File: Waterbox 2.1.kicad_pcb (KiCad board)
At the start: 2 copper layers, 130.2 x 78.5 mm, 25 parts

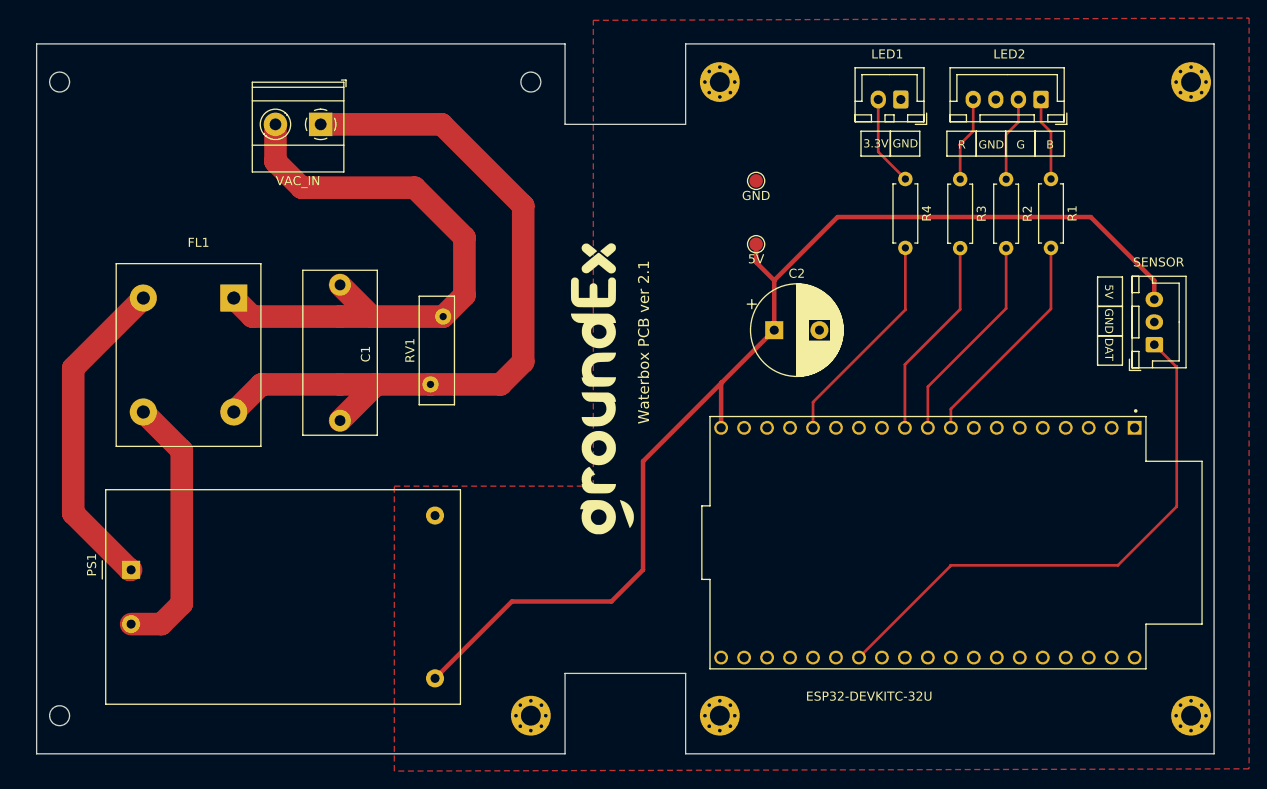
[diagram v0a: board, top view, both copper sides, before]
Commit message: route tracks in back copper, adding dc jack for additional dc power connector
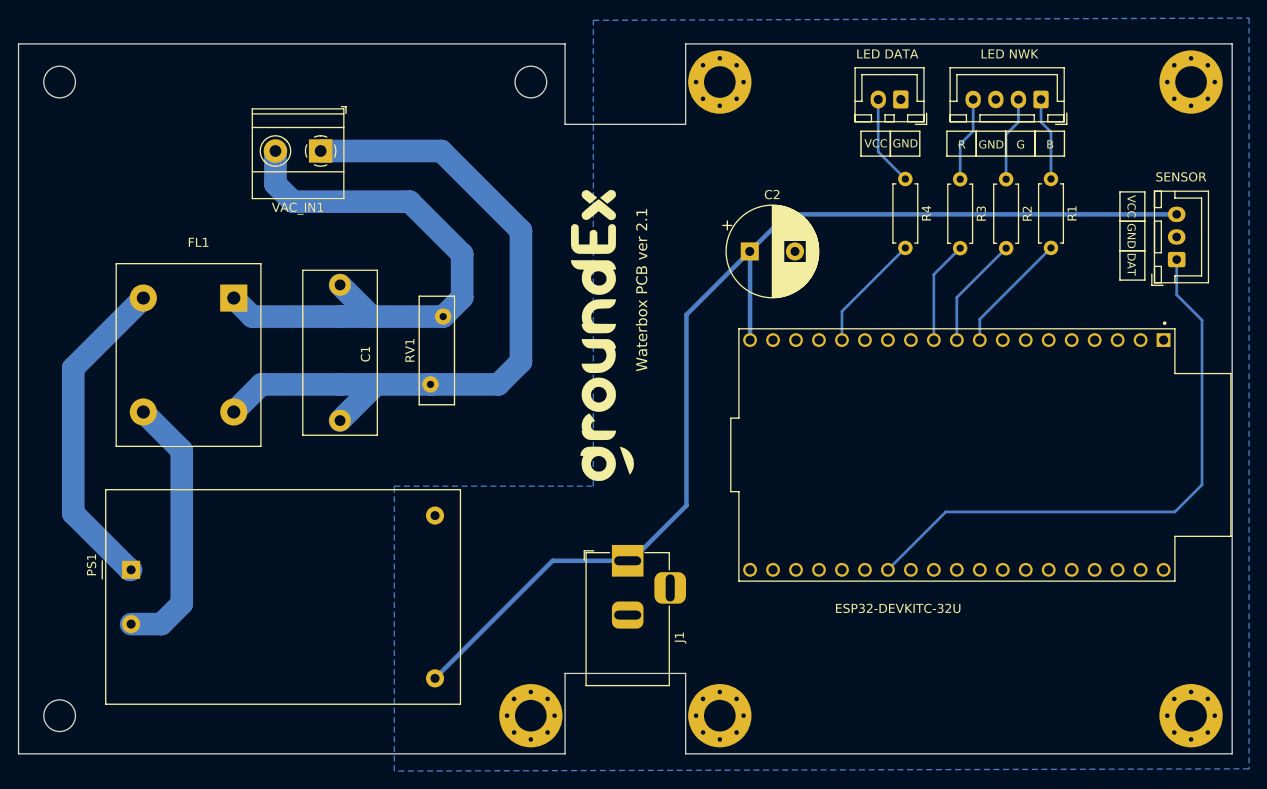
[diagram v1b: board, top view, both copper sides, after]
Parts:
- removed 5V: TP1, TestPoint:TestPoint_Pad_D1.5mm
- removed GND: TP2, TestPoint:TestPoint_Pad_D1.5mm
- added J1: Jack-DC, Connector_BarrelJack:BarrelJack_Horizontal, F.Cu at (125.8, 110.0)
- H1, H2, H3: footprint MountingHole:MountingHole_2.2mm_M2_ISO14580 -> MountingHole:MountingHole_3.5mm
- H4, H5, H6, H7, H8: footprint MountingHole:MountingHole_2.2mm_M2_Pad_Via -> MountingHole:MountingHole_3.5mm_Pad_Via
- LED DATA: renamed from LED1
- LED NWK: renamed from LED2
- moved ESP32-DEVKITC-32U 10.2 mm to (162.2, 98.3)
- moved SENSOR 9.73 mm to (186.5, 76.7)
- moved C2 9.11 mm to (139.3, 75.8)
- moved G*** 5.90 mm to (123.0, 85.1)
- moved VAC_IN1 2.94 mm to (91.9, 64.7)
- renumbered VAC_IN to VAC_IN1
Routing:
- net /LED_TEL: track 24.1 -> 13.1 mm
- net /RGBLED_R: track 22.4 -> 11.4 mm
- net /RGBLED_B: track 24.5 -> 13.4 mm
- net /RGBLED_G: track 23.4 -> 12.4 mm
- net /Sensor_Data: track 61.1 -> 64.7 mm
- net Net-(VAC_IN1-Pin_1): track 83.3 -> 80.0 mm
- net Net-(VAC_IN1-Pin_2): track 67.4 -> 64.5 mm
- added copper zone on B.Cu, net GND
- removed copper zone on F.Cu, net GND
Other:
- board size 130.2 x 78.5 mm -> 134.2 x 78.5 mm
- board text added: "VCC"
- board text removed: "3.3V"
- board text removed: "5V"
